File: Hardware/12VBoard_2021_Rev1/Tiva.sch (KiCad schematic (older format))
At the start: 1 part

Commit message: current sense
finished adding current sensing to high current side, also started thinking about tiva pin connector layout
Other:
- note added: "Aux Mount CTL"
- note added: "Aux Mount Sense"
- note added: "Camera CTL"
- note added: "Drive Sense"
- note added: "Extra (LowC) Sense"
- note added: "Extra CTL"
- note added: "Multimedia Sense"
- note added: "Multimedia/Extra CTL"
- note added: "NavBoard CTL"
- moved on the sheet: Conn?
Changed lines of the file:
@@
 L MRDT_Connectors:Molex_SL_10 Conn?
 U 1 1 5F9BCEA4
-P 4250 3100
-F 0 "Conn?" H 4378 3658 60  0000 L CNN
-F 1 "Molex_SL_10" H 4378 3552 60  0000 L CNN
-F 2 "" H 4250 3600 60  0001 C CNN
-F 3 "" H 4250 3600 60  0001 C CNN
-	1    4250 3100
+P 6550 4600
+F 0 "Conn?" H 6678 5158 60  0000 L CNN
+F 1 "Molex_SL_10" H 6678 5052 60  0000 L CNN
+F 2 "" H 6550 5100 60  0001 C CNN
+F 3 "" H 6550 5100 60  0001 C CNN
+	1    6550 4600
 	1    0    0    -1
 $EndComp
-Text Notes 4400 2950 0    79   ~ 0
+Text Notes 5850 4950 0    79   ~ 0
 Tiva 4 analog(current sense)/ \n5 toggles(digital write)
+Text Notes 5850 4550 0    50   ~ 0
+Drive Sense
+Text Notes 5650 4450 0    50   ~ 0
+Aux Mount Sense
+Text Notes 5650 4350 0    50   ~ 0
+Multimedia Sense
+Text Notes 5550 4250 0    50   ~ 0
+Extra (LowC) Sense
+Text Notes 5850 3950 0    50   ~ 0
+Camera CTL
+Text Notes 5800 4050 0    50   ~ 0
+NavBoard CTL
+Text Notes 5950 4150 0    50   ~ 0
+Extra CTL
+Text Notes 5750 3750 0    50   ~ 0
+Aux Mount CTL
+Text Notes 5500 3850 0    50   ~ 0
+Multimedia/Extra CTL
 $EndSCHEMATC

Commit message: Ferite bead?
MERGE?????
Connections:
- net DriveSense: now reaches Conn?.1
- net AuxCTL: now reaches Conn?.10
- net AuxMountSense: now reaches Conn?.2
- net MulitmediaSense: now reaches Conn?.3
- net LowCurrentSense: now reaches Conn?.4
- net GimbalCTL: now reaches Conn?.6
- net NavBoardCTL: now reaches Conn?.7
- net CameraCTL: now reaches Conn?.8
- net MultimediaCTL: now reaches Conn?.9
- no-connect marks 0 -> 1
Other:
- note added: "Extra Pin"
- note added: "Gimbal CTL"
- note removed: "Extra CTL"
- moved on the sheet: Conn?
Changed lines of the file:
@@
 $Descr A4 11693 8268
 encoding utf-8
-Sheet 2 13
+Sheet 2 8
 Title ""
 Date ""
@@
 L MRDT_Connectors:Molex_SL_10 Conn?
 U 1 1 5F9BCEA4
-P 6550 4600
-F 0 "Conn?" H 6678 5158 60  0000 L CNN
-F 1 "Molex_SL_10" H 6678 5052 60  0000 L CNN
-F 2 "" H 6550 5100 60  0001 C CNN
-F 3 "" H 6550 5100 60  0001 C CNN
-	1    6550 4600
+P 6600 4650
+F 0 "Conn?" H 6400 5825 60  0000 L CNN
+F 1 "Molex_SL_10" H 6400 5725 60  0000 L CNN
+F 2 "" H 6600 5150 60  0001 C CNN
+F 3 "" H 6600 5150 60  0001 C CNN
+	1    6600 4650
 	1    0    0    -1
 $EndComp
 Text Notes 5850 4950 0    79   ~ 0
 Tiva 4 analog(current sense)/ \n5 toggles(digital write)
-Text Notes 5850 4550 0    50   ~ 0
+Text Notes 7175 3725 2    50   ~ 0
 Drive Sense
-Text Notes 5650 4450 0    50   ~ 0
+Text Notes 7375 3825 2    50   ~ 0
 Aux Mount Sense
-Text Notes 5650 4350 0    50   ~ 0
+Text Notes 7400 3925 2    50   ~ 0
 Multimedia Sense
-Text Notes 5550 4250 0    50   ~ 0
+Text Notes 7475 4025 2    50   ~ 0
 Extra (LowC) Sense
-Text Notes 5850 3950 0    50   ~ 0
+Text Notes 7175 4425 2    50   ~ 0
 Camera CTL
-Text Notes 5800 4050 0    50   ~ 0
+Text Notes 7250 4325 2    50   ~ 0
 NavBoard CTL
-Text Notes 5950 4150 0    50   ~ 0
-Extra CTL
-Text Notes 5750 3750 0    50   ~ 0
+Text Notes 7075 4125 2    50   ~ 0
+Extra Pin
+Text Notes 7300 4625 2    50   ~ 0
 Aux Mount CTL
-Text Notes 5500 3850 0    50   ~ 0
+Text Notes 7550 4525 2    50   ~ 0
 Multimedia/Extra CTL
+Text Notes 6725 4225 0    49   ~ 0
+Gimbal CTL
+Text HLabel 6050 3700 0    49   Output ~ 0
+DriveSense
+Wire Wire Line
+	6400 3700 6050 3700
+Text HLabel 6050 3800 0    49   Output ~ 0
+AuxMountSense
+Wire Wire Line
+	6400 3800 6050 3800
+Text HLabel 6050 3900 0    49   Output ~ 0
+MulitmediaSense
+Wire Wire Line
+	6400 3900 6050 3900
+Text HLabel 6050 4000 0    49   Output ~ 0
+LowCurrentSense
+Wire Wire Line
+	6400 4000 6050 4000
+Text HLabel 6050 4200 0    49   Output ~ 0
+GimbalCTL
+Wire Wire Line
+	6400 4200 6050 4200
+Text HLabel 6050 4300 0    49   Output ~ 0
+NavBoardCTL
+Wire Wire Line
+	6400 4300 6050 4300
+Text HLabel 6050 4400 0    49   Output ~ 0
+CameraCTL
+Wire Wire Line
+	6400 4400 6050 4400
+Text HLabel 6050 4500 0    49   Output ~ 0
+MultimediaCTL
+Wire Wire Line
+	6400 4500 6050 4500
+Text HLabel 6050 4600 0    49   Output ~ 0
+AuxCTL
+Wire Wire Line
+	6400 4600 6050 4600
+NoConn ~ 6400 4100
 $EndSCHEMATC

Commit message: High current
Fisnished adding labes/tags
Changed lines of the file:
@@
 Text Notes 6725 4225 0    49   ~ 0
 Gimbal CTL
-Text HLabel 6050 3700 0    49   Output ~ 0
+Text HLabel 6050 3700 0    49   Input ~ 0
 DriveSense
 Wire Wire Line
 	6400 3700 6050 3700
-Text HLabel 6050 3800 0    49   Output ~ 0
+Text HLabel 6050 3800 0    49   Input ~ 0
 AuxMountSense
 Wire Wire Line
 	6400 3800 6050 3800
-Text HLabel 6050 3900 0    49   Output ~ 0
+Text HLabel 6050 3900 0    49   Input ~ 0
 MulitmediaSense
 Wire Wire Line
 	6400 3900 6050 3900
-Text HLabel 6050 4000 0    49   Output ~ 0
+Text HLabel 6050 4000 0    49   Input ~ 0
 LowCurrentSense
 Wire Wire Line
 	6400 4000 6050 4000
-Text HLabel 6050 4200 0    49   Output ~ 0
-GimbalCTL
 Wire Wire Line
 	6400 4200 6050 4200
-Text HLabel 6050 4300 0    49   Output ~ 0
-NavBoardCTL
 Wire Wire Line
 	6400 4300 6050 4300
@@
 	6400 4600 6050 4600
 NoConn ~ 6400 4100
+Text HLabel 6050 4300 0    49   Output ~ 0
+NavBoardCTL
+Text HLabel 6050 4200 0    49   Output ~ 0
+GimbalCTL
 $EndSCHEMATC

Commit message: Changed things
Dans a quitter
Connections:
- net ExtraCTL: now reaches Conn?.5
- no-connect marks 1 -> 0
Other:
- note added: "Extra CTL"
- note removed: "Extra Pin"
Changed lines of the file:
@@
 NavBoard CTL
 Text Notes 7075 4125 2    50   ~ 0
-Extra Pin
+Extra CTL
 Text Notes 7300 4625 2    50   ~ 0
 Aux Mount CTL
@@
 Wire Wire Line
 	6400 4600 6050 4600
-NoConn ~ 6400 4100
 Text HLabel 6050 4300 0    49   Output ~ 0
 NavBoardCTL
 Text HLabel 6050 4200 0    49   Output ~ 0
 GimbalCTL
+Text HLabel 6050 4100 0    49   Output ~ 0
+ExtraCTL
+Wire Wire Line
+	6400 4100 6050 4100
 $EndSCHEMATC

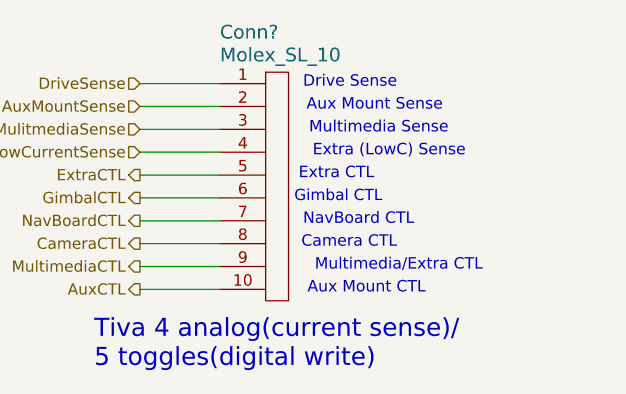
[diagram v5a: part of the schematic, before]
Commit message: fixed High current for second review
addes gimbal to high current. added teva digital write pin to gimbal fot CTL. changed ports from 15 to 10 amp
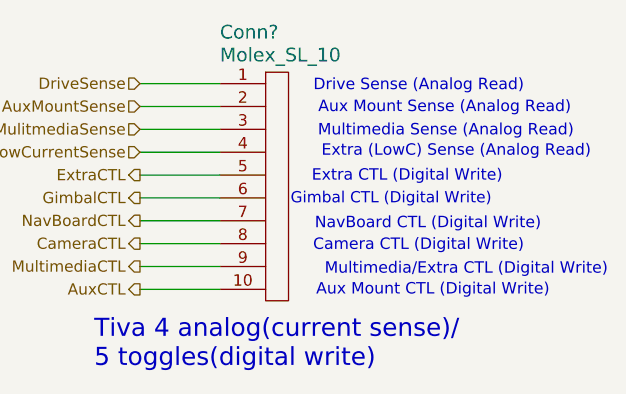
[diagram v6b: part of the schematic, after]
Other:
- note added: "Aux Mount CTL (Digital Write)"
- note added: "Aux Mount Sense (Analog Read)"
- note added: "Camera CTL (Digital Write)"
- note added: "Drive Sense (Analog Read)"
- note added: "Extra (LowC) Sense (Analog Read)"
- note added: "Extra CTL (Digital Write)"
- note added: "Gimbal CTL (Digital Write)"
- note added: "Multimedia Sense (Analog Read)"
- note added: "Multimedia/Extra CTL (Digital Write)"
- note added: "NavBoard CTL (Digital Write)"
- note removed: "Aux Mount CTL"
- note removed: "Aux Mount Sense"
- note removed: "Camera CTL"
- note removed: "Drive Sense"
- note removed: "Extra (LowC) Sense"
- note removed: "Extra CTL"
- note removed: "Gimbal CTL"
- note removed: "Multimedia Sense"
- note removed: "Multimedia/Extra CTL"
- note removed: "NavBoard CTL"
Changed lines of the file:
@@
 $Descr A4 11693 8268
 encoding utf-8
-Sheet 2 7
+Sheet 2 8
 Title ""
 Date ""
@@
 Text Notes 5850 4950 0    79   ~ 0
 Tiva 4 analog(current sense)/ \n5 toggles(digital write)
-Text Notes 7175 3725 2    50   ~ 0
-Drive Sense
-Text Notes 7375 3825 2    50   ~ 0
-Aux Mount Sense
-Text Notes 7400 3925 2    50   ~ 0
-Multimedia Sense
-Text Notes 7475 4025 2    50   ~ 0
-Extra (LowC) Sense
-Text Notes 7175 4425 2    50   ~ 0
-Camera CTL
-Text Notes 7250 4325 2    50   ~ 0
-NavBoard CTL
-Text Notes 7075 4125 2    50   ~ 0
-Extra CTL
-Text Notes 7300 4625 2    50   ~ 0
-Aux Mount CTL
-Text Notes 7550 4525 2    50   ~ 0
-Multimedia/Extra CTL
-Text Notes 6725 4225 0    49   ~ 0
-Gimbal CTL
+Text Notes 7730 3740 2    50   ~ 0
+Drive Sense (Analog Read)
+Text Notes 7936 3836 2    50   ~ 0
+Aux Mount Sense (Analog Read)
+Text Notes 7948 3938 2    50   ~ 0
+Multimedia Sense (Analog Read)
+Text Notes 8023 4027 2    50   ~ 0
+Extra (LowC) Sense (Analog Read)
+Text Notes 7730 4439 2    50   ~ 0
+Camera CTL (Digital Write)
+Text Notes 7805 4344 2    50   ~ 0
+NavBoard CTL (Digital Write)
+Text Notes 7636 4136 2    50   ~ 0
+Extra CTL (Digital Write)
+Text Notes 7842 4634 2    50   ~ 0
+Aux Mount CTL (Digital Write)
+Text Notes 8097 4543 2    50   ~ 0
+Multimedia/Extra CTL (Digital Write)
+Text Notes 6709 4235 0    49   ~ 0
+Gimbal CTL (Digital Write)
 Text HLabel 6050 3700 0    49   Input ~ 0
 DriveSense

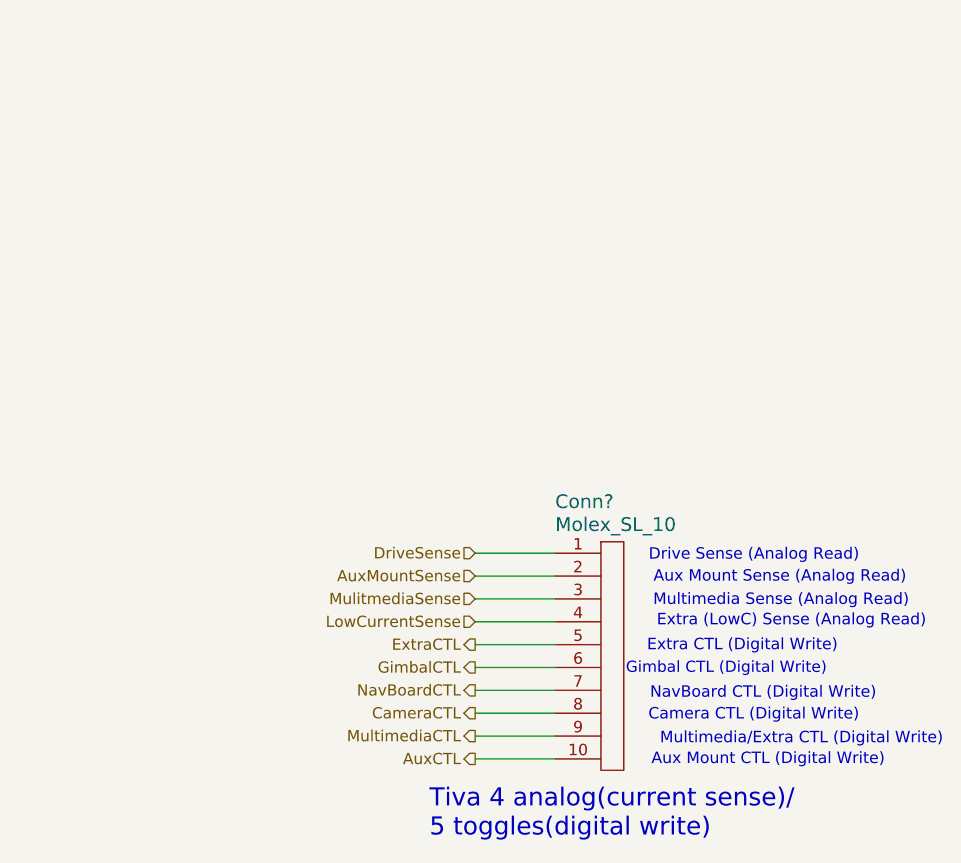
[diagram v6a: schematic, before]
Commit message: Connector change
added current sense to gimbal and changed tiva header to two molex connectors to allow for more pins
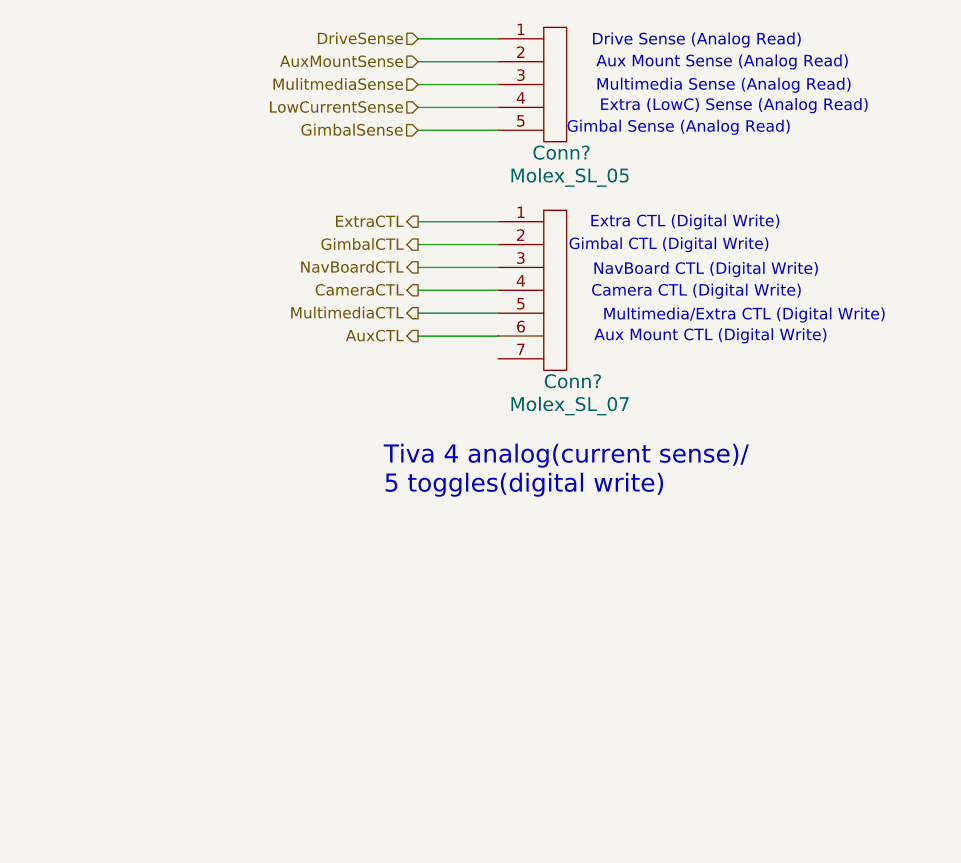
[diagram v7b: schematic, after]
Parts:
- removed Conn?: Molex_SL_10, symbol MRDT_Connectors:Molex_SL_10
- added Conn?: Molex_SL_05, symbol MRDT_Connectors:Molex_SL_05
- added Conn?: Molex_SL_07, symbol MRDT_Connectors:Molex_SL_07
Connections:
- net AuxCTL: now also Conn?.6
- net AuxMountSense: now also Conn?.2
- net CameraCTL: now also Conn?.4
- net DriveSense: now also Conn?.1
- net ExtraCTL: now also Conn?.1
- net GimbalCTL: now also Conn?.2
- net LowCurrentSense: now also Conn?.4
- net MulitmediaSense: now also Conn?.3
- net MultimediaCTL: now also Conn?.5
- net NavBoardCTL: now also Conn?.3
- new net GimbalSense: Conn?.5
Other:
- note added: "Gimbal Sense (Analog Read)"
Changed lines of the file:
@@
 Comment4 ""
 $EndDescr
+Text Notes 5650 3450 0    79   ~ 0
+Tiva 4 analog(current sense)/ \n5 toggles(digital write)
+Text Notes 7480 1490 2    50   ~ 0
+Drive Sense (Analog Read)
+Text Notes 7686 1586 2    50   ~ 0
+Aux Mount Sense (Analog Read)
+Text Notes 7698 1688 2    50   ~ 0
+Multimedia Sense (Analog Read)
+Text Notes 7773 1777 2    50   ~ 0
+Extra (LowC) Sense (Analog Read)
+Text Notes 7480 2589 2    50   ~ 0
+Camera CTL (Digital Write)
+Text Notes 7555 2494 2    50   ~ 0
+NavBoard CTL (Digital Write)
+Text Notes 7386 2286 2    50   ~ 0
+Extra CTL (Digital Write)
+Text Notes 7592 2784 2    50   ~ 0
+Aux Mount CTL (Digital Write)
+Text Notes 7847 2693 2    50   ~ 0
+Multimedia/Extra CTL (Digital Write)
+Text Notes 6459 2385 0    49   ~ 0
+Gimbal CTL (Digital Write)
+Text HLabel 5800 1450 0    49   Input ~ 0
+DriveSense
+Wire Wire Line
+	6150 1450 5800 1450
+Text HLabel 5800 1550 0    49   Input ~ 0
+AuxMountSense
+Wire Wire Line
+	6150 1550 5800 1550
+Text HLabel 5800 1650 0    49   Input ~ 0
+MulitmediaSense
+Wire Wire Line
+	6150 1650 5800 1650
+Text HLabel 5800 1750 0    49   Input ~ 0
+LowCurrentSense
+Wire Wire Line
+	6150 1750 5800 1750
+Wire Wire Line
+	6150 2350 5800 2350
+Wire Wire Line
+	6150 2450 5800 2450
+Text HLabel 5800 2550 0    49   Output ~ 0
+CameraCTL
+Wire Wire Line
+	6150 2550 5800 2550
+Text HLabel 5800 2650 0    49   Output ~ 0
+MultimediaCTL
+Wire Wire Line
+	6150 2650 5800 2650
+Text HLabel 5800 2750 0    49   Output ~ 0
+AuxCTL
+Wire Wire Line
+	6150 2750 5800 2750
+Text HLabel 5800 2450 0    49   Output ~ 0
+NavBoardCTL
+Text HLabel 5800 2350 0    49   Output ~ 0
+GimbalCTL
+Text HLabel 5800 2250 0    49   Output ~ 0
+ExtraCTL
+Wire Wire Line
+	6150 2250 5800 2250
 $Comp
-L MRDT_Connectors:Molex_SL_10 Conn?
-U 1 1 5F9BCEA4
-P 6600 4650
-F 0 "Conn?" H 6400 5825 60  0000 L CNN
-F 1 "Molex_SL_10" H 6400 5725 60  0000 L CNN
-F 2 "" H 6600 5150 60  0001 C CNN
-F 3 "" H 6600 5150 60  0001 C CNN
-	1    6600 4650
+L MRDT_Connectors:Molex_SL_05 Conn?
+U 1 1 5F976F73
+P 6350 1900
+F 0 "Conn?" H 6300 1850 60  0000 L CNN
+F 1 "Molex_SL_05" H 6200 1750 60  0000 L CNN
+F 2 "" H 6350 1900 60  0001 C CNN
+F 3 "" H 6350 1900 60  0001 C CNN
+	1    6350 1900
 	1    0    0    -1
 $EndComp
-Text Notes 5850 4950 0    79   ~ 0
-Tiva 4 analog(current sense)/ \n5 toggles(digital write)
-Text Notes 7730 3740 2    50   ~ 0
-Drive Sense (Analog Read)
-Text Notes 7936 3836 2    50   ~ 0
-Aux Mount Sense (Analog Read)
-Text Notes 7948 3938 2    50   ~ 0
-Multimedia Sense (Analog Read)
-Text Notes 8023 4027 2    50   ~ 0
-Extra (LowC) Sense (Analog Read)
-Text Notes 7730 4439 2    50   ~ 0
-Camera CTL (Digital Write)
-Text Notes 7805 4344 2    50   ~ 0
-NavBoard CTL (Digital Write)
-Text Notes 7636 4136 2    50   ~ 0
-Extra CTL (Digital Write)
-Text Notes 7842 4634 2    50   ~ 0
-Aux Mount CTL (Digital Write)
-Text Notes 8097 4543 2    50   ~ 0
-Multimedia/Extra CTL (Digital Write)
-Text Notes 6709 4235 0    49   ~ 0
-Gimbal CTL (Digital Write)
-Text HLabel 6050 3700 0    49   Input ~ 0
-DriveSense
+$Comp
+L MRDT_Connectors:Molex_SL_07 Conn?
+U 1 1 5F97771C
+P 6350 2900
+F 0 "Conn?" H 6350 2850 60  0000 L CNN
+F 1 "Molex_SL_07" H 6200 2750 60  0000 L CNN
+F 2 "" H 6350 3100 60  0001 C CNN
+F 3 "" H 6350 3100 60  0001 C CNN
+	1    6350 2900
+	1    0    0    -1
+$EndComp
+Text HLabel 5800 1850 0    50   Input ~ 0
+GimbalSense
 Wire Wire Line
-	6400 3700 6050 3700
-Text HLabel 6050 3800 0    49   Input ~ 0
-AuxMountSense
-Wire Wire Line
-	6400 3800 6050 3800
-Text HLabel 6050 3900 0    49   Input ~ 0
-MulitmediaSense
-Wire Wire Line
-	6400 3900 6050 3900
-Text HLabel 6050 4000 0    49   Input ~ 0
-LowCurrentSense
-Wire Wire Line
-	6400 4000 6050 4000
-Wire Wire Line
-	6400 4200 6050 4200
-Wire Wire Line
-	6400 4300 6050 4300
-Text HLabel 6050 4400 0    49   Output ~ 0
-CameraCTL
-Wire Wire Line
-	6400 4400 6050 4400
-Text HLabel 6050 4500 0    49   Output ~ 0
-MultimediaCTL
-Wire Wire Line
-	6400 4500 6050 4500
-Text HLabel 6050 4600 0    49   Output ~ 0
-AuxCTL
-Wire Wire Line
-	6400 4600 6050 4600
-Text HLabel 6050 4300 0    49   Output ~ 0
-NavBoardCTL
-Text HLabel 6050 4200 0    49   Output ~ 0
-GimbalCTL
-Text HLabel 6050 4100 0    49   Output ~ 0
-ExtraCTL
-Wire Wire Line
-	6400 4100 6050 4100
+	6150 1850 5800 1850
+Text Notes 6450 1872 0    50   ~ 0
+Gimbal Sense (Analog Read)
 $EndSCHEMATC

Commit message: fixed some stuffs
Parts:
- Conn2: renamed from Conn?; footprint (none) -> MRDT_Connectors:MOLEX_SL_05_Horizontal
- Conn3: renamed from Conn?; footprint (none) -> MRDT_Connectors:MOLEX_SL_07_Horizontal
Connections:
- no-connect marks 0 -> 1
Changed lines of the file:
@@
 	6150 2250 5800 2250
 $Comp
-L MRDT_Connectors:Molex_SL_05 Conn?
+L MRDT_Connectors:Molex_SL_05 Conn2
 U 1 1 5F976F73
 P 6350 1900
-F 0 "Conn?" H 6300 1850 60  0000 L CNN
+F 0 "Conn2" H 6300 1850 60  0000 L CNN
 F 1 "Molex_SL_05" H 6200 1750 60  0000 L CNN
-F 2 "" H 6350 1900 60  0001 C CNN
+F 2 "MRDT_Connectors:MOLEX_SL_05_Horizontal" H 6350 1900 60  0001 C CNN
 F 3 "" H 6350 1900 60  0001 C CNN
 	1    6350 1900
@@
 $EndComp
 $Comp
-L MRDT_Connectors:Molex_SL_07 Conn?
+L MRDT_Connectors:Molex_SL_07 Conn3
 U 1 1 5F97771C
 P 6350 2900
-F 0 "Conn?" H 6350 2850 60  0000 L CNN
+F 0 "Conn3" H 6350 2850 60  0000 L CNN
 F 1 "Molex_SL_07" H 6200 2750 60  0000 L CNN
-F 2 "" H 6350 3100 60  0001 C CNN
+F 2 "MRDT_Connectors:MOLEX_SL_07_Horizontal" H 6350 3100 60  0001 C CNN
 F 3 "" H 6350 3100 60  0001 C CNN
 	1    6350 2900
@@
 Text Notes 6450 1872 0    50   ~ 0
 Gimbal Sense (Analog Read)
+NoConn ~ 6150 2850
 $EndSCHEMATC
